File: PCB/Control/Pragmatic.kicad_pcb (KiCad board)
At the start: 2 copper layers, 44.5 x 35.6 mm, 7 parts, among them J1 L, J2 R, J3 Conn_01x04, SW1 SW_Push, U1 ProMicro

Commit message: build instruction draft
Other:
- board text added: "Pragmatic Keyboard Kit Control Module Design by James Sa V0.3 2021-11-29"
- board text removed: "Pragmatic Keyboard Kit Bridge Module Design by James Sa V0.3 2021-11-29"
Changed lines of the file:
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@@
     (descr https://www.omron.com/ecb/products/pdf/en-b3f.pdf)
     (tags "tact sw push 6mm")
+    (attr smd)
     (fp_text reference SW1 (at 3.25 2.214) (layer F.SilkS) hide
       (effects (font (size 1 1) (thickness 0.15)))
@@
     (descr "Through hole IDC box header, 2x07, 2.54mm pitch, DIN 41651 / IEC 60603-13, double rows, https://docs.google.com/spreadsheets/d/16SsEcesNF15N3Lb4niX7dcUr-NY5_MFPQhobNuNppn4/edit#gid=0")
     (tags "Through hole vertical IDC box header THT 2x07 2.54mm double row")
+    (attr smd)
     (fp_text reference J2 (at 1.27 -2.54) (layer F.SilkS)
       (effects (font (size 1.016 1.016) (thickness 0.1778)))
@@
     (descr "Through hole IDC box header, 2x07, 2.54mm pitch, DIN 41651 / IEC 60603-13, double rows, https://docs.google.com/spreadsheets/d/16SsEcesNF15N3Lb4niX7dcUr-NY5_MFPQhobNuNppn4/edit#gid=0")
     (tags "Through hole vertical IDC box header THT 2x07 2.54mm double row")
+    (attr smd)
     (fp_text reference J1 (at 1.27 -2.54) (layer F.SilkS)
       (effects (font (size 1.016 1.016) (thickness 0.1778)))
@@
     (effects (font (size 1.016 1.016) (thickness 0.1778) italic))
   )
-  (gr_text "Pragmatic Keyboard Kit\nBridge Module\nDesign by James Sa\nV0.3 2021-11-29" (at 139.7 50.8 90) (layer B.SilkS)
+  (gr_text "Pragmatic Keyboard Kit\nControl Module\nDesign by James Sa\nV0.3 2021-11-29" (at 139.7 50.8 90) (layer B.SilkS)
     (effects (font (size 1.016 1.016) (thickness 0.1778)) (justify left mirror))
   )

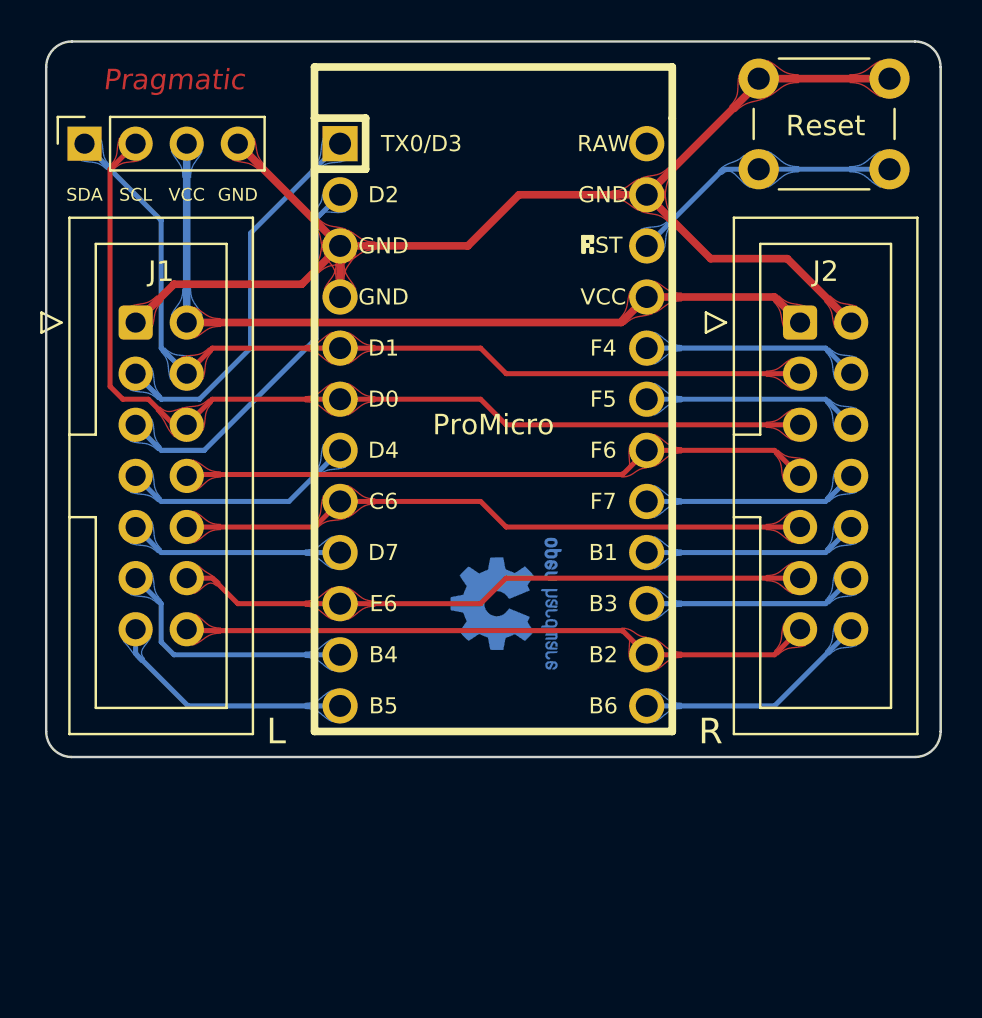
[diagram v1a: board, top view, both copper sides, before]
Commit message: migrate to Kicad 6
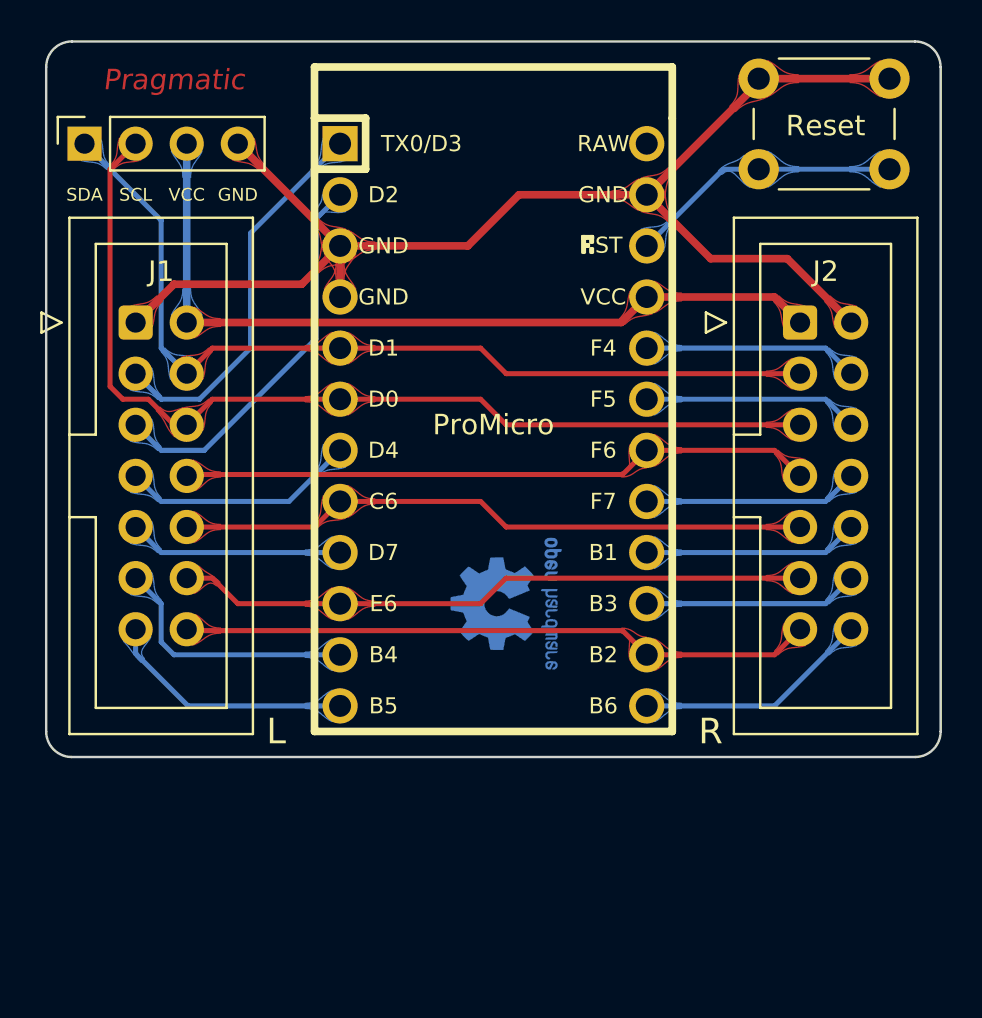
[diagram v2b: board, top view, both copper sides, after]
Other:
- net class Default removed
- net class Power removed

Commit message: v2
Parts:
- removed J3: Conn_01x04, Connector_PinSocket_2.54mm:PinSocket_1x04_P2.54mm_Vertical
- added REF**: JLC Legend, Keyboard_JSA:JLC Legend, F.Cu at (156.2, 48.3)
- moved Logo1 26.3 mm to (124.5, 51.4)
- moved J2 15.5 mm to (157.5, 73.7), turned to 180 degrees
- moved Logo2 12.5 mm to (141.0, 72.4)
- moved SW1 0.30 mm to (159.5, 50.5)
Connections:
- J1 pad 1: GND -> VCC
- J1 pad 10: Row4 -> Col4
- J1 pad 11: Col5 -> Row5
- J1 pad 12: Row5 -> Col5
- J1 pad 13: Col6 -> Row6
- J1 pad 14: Row6 -> Col6
- J1 pad 2: VCC -> GND
- J1 pad 3: Col1 -> Row1
- J1 pad 4: Row1 -> Col1
- J1 pad 5: Col2 -> Row2
- J1 pad 6: Row2 -> Col2
- J1 pad 7: Col3 -> Row3
- J1 pad 8: Row3 -> Col3
- J1 pad 9: Col4 -> Row4
- J2 pad 10: Col9 -> Col10
- J2 pad 12: Col8 -> Col11
- J2 pad 14: Col7 -> Col12
- J2 pad 4: Col12 -> Col7
- J2 pad 6: Col11 -> Col8
- J2 pad 8: Col10 -> Col9
- U1 pad 24: (no net) -> unconnected-(U1-Pad24)
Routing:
- net Row6: track 31.5 -> 54.6 mm
- net VCC: track 40.4 -> 57.9 mm
- net Row3: track 31.5 -> 42.6 mm
- net Row5: track 31.5 -> 41.9 mm
- net Row2: track 49.4 -> 40.1 mm, vias 0 -> 2
- net Row4: track 31.5 -> 38.7 mm
- net GND: track 65.1 -> 72.3 mm
- net Reset: track 13.6 -> 7.34 mm
- net Col2: track 19.4 -> 14.6 mm
- net Col1: track 19.3 -> 14.6 mm
- net Col5: track 12.9 -> 9.20 mm
- net Col3: track 11.7 -> 8.15 mm
- net Col6: track 12.4 -> 9.20 mm
- net Col12: track 10.7 -> 8.15 mm
- net Col11: track 10.7 -> 8.15 mm
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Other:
- board text added: "Pragmatic Keyboard Kit Control Module Design by James Sa V2 2022-02-04"
- board text removed: "GND"
- board text removed: "Pragmatic Keyboard Kit Control Module Design by James Sa V0.3 2021-11-29"
- board text removed: "SCL"
- board text removed: "SDA"
- board text removed: "VCC"

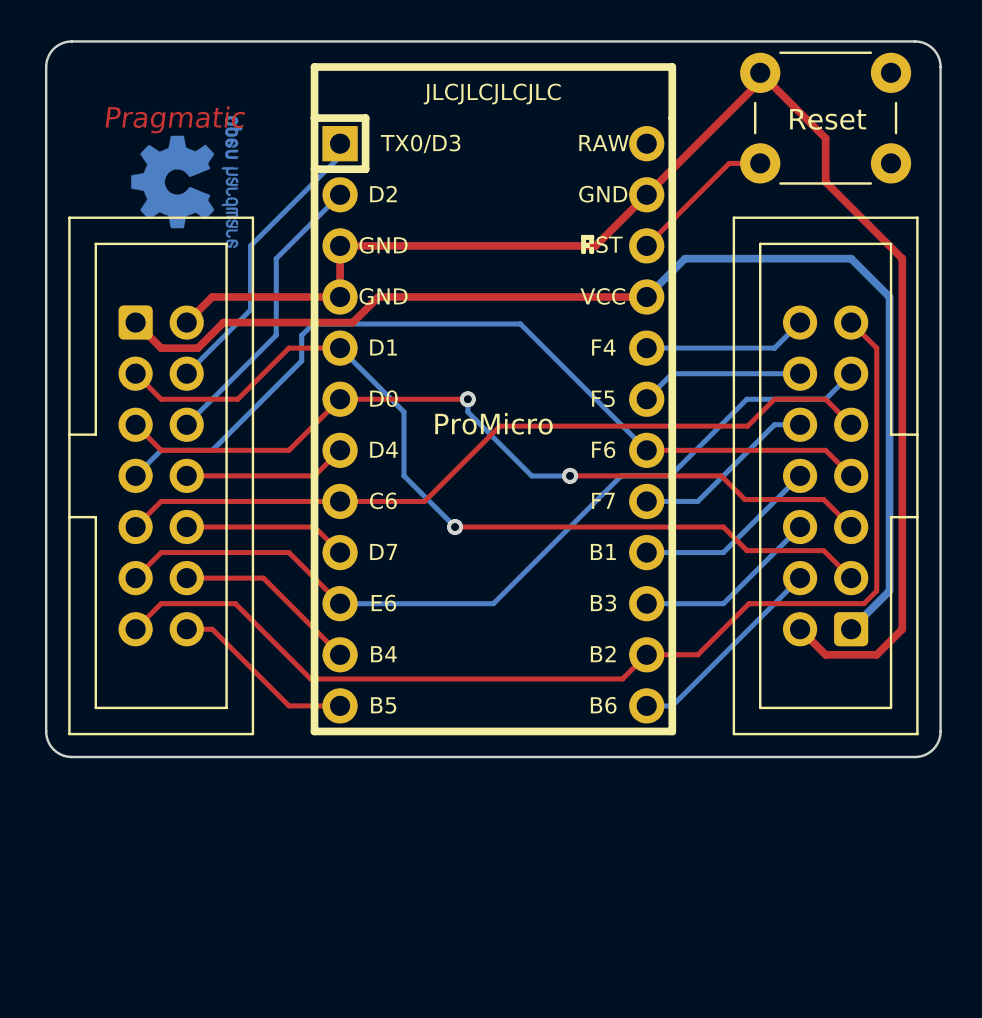
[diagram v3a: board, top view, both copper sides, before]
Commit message: add elite C extension
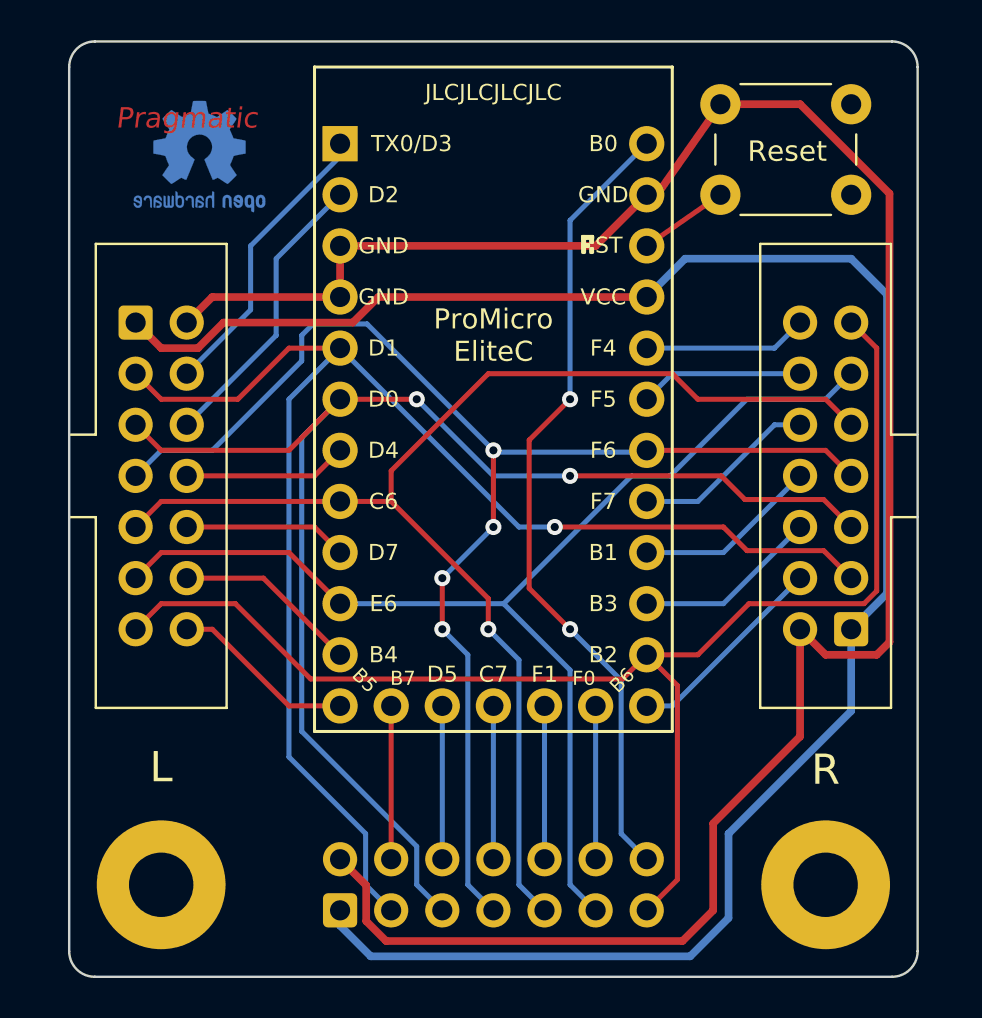
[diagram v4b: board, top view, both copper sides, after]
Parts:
- removed Logo2: KiCad-Logo_5mm_SilkScreen, Symbol:KiCad-Logo_5mm_SilkScreen
- removed the REF** at (156.2, 48.3)
- added J3: M, Connector_IDC:IDC-Header_2x07_P2.54mm_Vertical, F.Cu at (132.1, 87.6)
- added L1: JLC Legend, Keyboard_JSA:JLC Legend, F.Cu at (139.7, 47.0)
- added M1: MountingHole_3.2mm_M3_Pad, MountingHole:MountingHole_3.2mm_M3_Pad, F.Cu at (123.2, 86.4)
- added M2: MountingHole_3.2mm_M3_Pad, MountingHole:MountingHole_3.2mm_M3_Pad, F.Cu at (156.2, 86.4)
- added REF**: KiCad-Logo_5mm_SilkScreen, Symbol:KiCad-Logo_5mm_SilkScreen, B.Cu at (140.0, 81.8)
- U1: value ProMicro -> ProMicro/Elite-C; footprint keyboards:ArduinoProMicro -> Keyboard_Keebio-Parts:Elite-C
- moved SW1 2.52 mm to (157.5, 52.1)
- moved Logo1 1.42 mm to (125.1, 50.2), turned to 180 degrees
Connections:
- U1 pad 24: unconnected-(U1-Pad24) -> Col18
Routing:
- net Col18: track 0.00 -> 40.4 mm, vias 0 -> 2
- net VCC: track 57.9 -> 96.2 mm
- net GND: track 72.3 -> 107.9 mm
- net Row1: track 43.7 -> 73.0 mm
- net Row2: track 40.1 -> 68.9 mm
- net Row4: track 38.7 -> 64.1 mm, vias 0 -> 1
- net Row3: track 42.6 -> 67.5 mm, vias 0 -> 4
- net Row5: track 41.9 -> 59.0 mm
- net Row6: track 54.6 -> 68.5 mm
- net Col17: track 0.00 -> 7.62 mm
- net Col16: track 0.00 -> 7.62 mm
- net Col15: track 0.00 -> 7.62 mm
- net Col14: track 0.00 -> 7.62 mm
- net Col13: track 0.00 -> 7.62 mm
- net Reset: track 7.34 -> 4.46 mm
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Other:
- board size 44.5 x 35.6 mm -> 42.2 x 46.5 mm
- board text added: "Pragmatic Keyboard Kit Control Module Design by James Sa V2.1 2022-02-07"
- board text added: "ProMicro EliteC"
- board text removed: "Pragmatic Keyboard Kit Control Module Design by James Sa V2 2022-02-04"
